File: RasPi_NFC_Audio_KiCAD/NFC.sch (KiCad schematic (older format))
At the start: 31 parts, among them U2 PN532, Y1 Oscillator

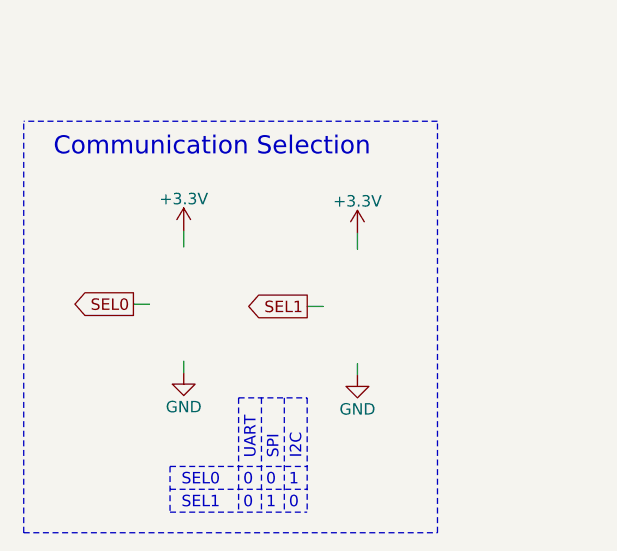
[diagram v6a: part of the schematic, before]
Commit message: Schematic updates
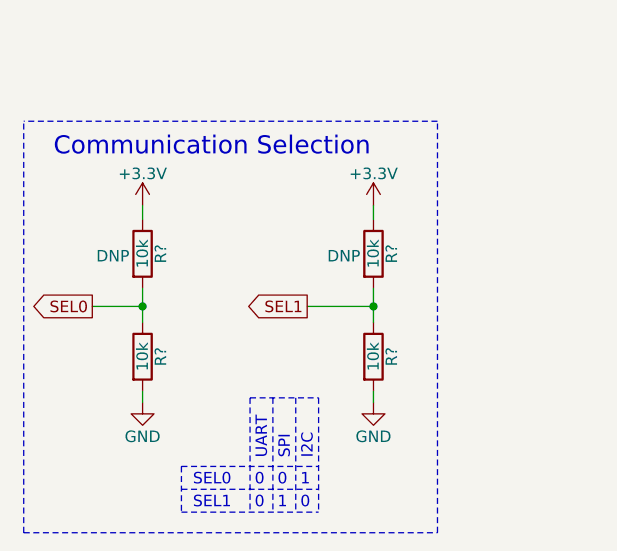
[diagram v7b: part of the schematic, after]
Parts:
- added R? (x4): 10k, Resistors_SMD:R_0603_HandSoldering, symbol Device:R
- L1, L2: DigiKey (none) -> 445-174193-1-ND; Part # (none) -> MLJ1608WR56JT000
- R6: DigiKey (none) -> 311-1.0KGRCT-ND; Part # (none) -> RC0603JR-071KL
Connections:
- wire segments 138 -> 142
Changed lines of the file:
@@
 EESchema Schematic File Version 4
 LIBS:RasPi_NFC_Audio_KiCAD-cache
-EELAYER 29 0
+EELAYER 30 0
 EELAYER END
 $Descr A4 11693 8268
@@
 F 2 "Inductors_SMD:L_0603_HandSoldering" H 8300 3440 50  0001 C CNN
 F 3 "" H 8300 3440 50  0001 C CNN
+F 4 "MLJ1608WR56JT000" H 8300 3440 50  0001 C CNN "Part #"
+F 5 "445-174193-1-ND" H 8300 3440 50  0001 C CNN "DigiKey"
 	1    8300 3440
 	0    -1   -1   0
@@
 F 2 "Inductors_SMD:L_0603_HandSoldering" H 8300 4390 50  0001 C CNN
 F 3 "" H 8300 4390 50  0001 C CNN
+F 4 "MLJ1608WR56JT000" H 8300 4390 50  0001 C CNN "Part #"
+F 5 "445-174193-1-ND" H 8300 4390 50  0001 C CNN "DigiKey"
 	1    8300 4390
 	0    -1   -1   0
@@
 F 2 "Resistors_SMD:R_0603_HandSoldering" V 7680 3090 50  0001 C CNN
 F 3 "" H 7750 3090 50  0001 C CNN
+F 4 "RC0603JR-071KL" H 7750 3090 50  0001 C CNN "Part #"
+F 5 "311-1.0KGRCT-ND" H 7750 3090 50  0001 C CNN "DigiKey"
 	1    7750 3090
 	0    1    1    0
@@
 Text GLabel 5250 3040 0    50   Input ~ 0
 SEL1
-Text GLabel 2160 6430 0    50   Output ~ 0
+Text GLabel 1980 6440 0    50   Output ~ 0
 SEL0
 $Comp
 L power:GND #PWR0127
 U 1 1 5E1B7458
-P 2380 6730
-F 0 "#PWR0127" H 2380 6480 50  0001 C CNN
-F 1 "GND" H 2380 6580 50  0000 C CNN
-F 2 "" H 2380 6730 50  0001 C CNN
-F 3 "" H 2380 6730 50  0001 C CNN
-	1    2380 6730
+P 2200 6860
+F 0 "#PWR0127" H 2200 6610 50  0001 C CNN
+F 1 "GND" H 2200 6710 50  0000 C CNN
+F 2 "" H 2200 6860 50  0001 C CNN
+F 3 "" H 2200 6860 50  0001 C CNN
+	1    2200 6860
 	1    0    0    -1
 $EndComp
@@
 L power:+3.3V #PWR0128
 U 1 1 5E1B7781
-P 2380 6110
-F 0 "#PWR0128" H 2380 5960 50  0001 C CNN
-F 1 "+3.3V" H 2380 6250 50  0000 C CNN
-F 2 "" H 2380 6110 50  0001 C CNN
-F 3 "" H 2380 6110 50  0001 C CNN
-	1    2380 6110
-	1    0    0    -1
-$EndComp
-Wire Wire Line
-	2160 6430 2230 6430
-Wire Wire Line
-	2380 6180 2380 6110
-Wire Wire Line
-	2380 6680 2380 6730
+P 2200 6000
+F 0 "#PWR0128" H 2200 5850 50  0001 C CNN
+F 1 "+3.3V" H 2200 6140 50  0000 C CNN
+F 2 "" H 2200 6000 50  0001 C CNN
+F 3 "" H 2200 6000 50  0001 C CNN
+	1    2200 6000
+	1    0    0    -1
+$EndComp
 Text GLabel 2920 6440 0    50   Output ~ 0
 SEL1
-$Comp
-L power:GND #PWR0129
-U 1 1 5E1D407F
-P 3140 6740
-F 0 "#PWR0129" H 3140 6490 50  0001 C CNN
-F 1 "GND" H 3140 6590 50  0000 C CNN
-F 2 "" H 3140 6740 50  0001 C CNN
-F 3 "" H 3140 6740 50  0001 C CNN
-	1    3140 6740
-	1    0    0    -1
-$EndComp
-$Comp
-L power:+3.3V #PWR0130
-U 1 1 5E1D4089
-P 3140 6120
-F 0 "#PWR0130" H 3140 5970 50  0001 C CNN
-F 1 "+3.3V" H 3140 6260 50  0000 C CNN
-F 2 "" H 3140 6120 50  0001 C CNN
-F 3 "" H 3140 6120 50  0001 C CNN
-	1    3140 6120
-	1    0    0    -1
-$EndComp
-Wire Wire Line
-	2920 6440 2990 6440
-Wire Wire Line
-	3140 6190 3140 6120
-Wire Wire Line
-	3140 6690 3140 6740
-Wire Notes Line
-	2320 7140 2320 7340
-Wire Notes Line
-	2320 7140 2920 7140
-Wire Notes Line
-	2320 7240 2920 7240
-Wire Notes Line
-	2320 7340 2920 7340
-Wire Notes Line
-	2620 6840 2920 6840
-Wire Notes Line
-	2620 6840 2620 7340
-Wire Notes Line
-	2920 6840 2920 7340
-Wire Notes Line
-	2820 6840 2820 7340
-Wire Notes Line
-	2720 6840 2720 7340
-Text Notes 2370 7230 0    50   ~ 0
+Wire Notes Line
+	2370 7140 2370 7340
+Wire Notes Line
+	2370 7140 2970 7140
+Wire Notes Line
+	2370 7240 2970 7240
+Wire Notes Line
+	2370 7340 2970 7340
+Wire Notes Line
+	2670 6840 2970 6840
+Wire Notes Line
+	2670 6840 2670 7340
+Wire Notes Line
+	2970 6840 2970 7340
+Wire Notes Line
+	2870 6840 2870 7340
+Wire Notes Line
+	2770 6840 2770 7340
+Text Notes 2420 7230 0    50   ~ 0
 SEL0
-Text Notes 2370 7330 0    50   ~ 0
+Text Notes 2420 7330 0    50   ~ 0
 SEL1
-Text Notes 2640 7330 0    50   ~ 0
+Text Notes 2690 7330 0    50   ~ 0
 0
-Text Notes 2640 7230 0    50   ~ 0
+Text Notes 2690 7230 0    50   ~ 0
 0
-Text Notes 2740 7230 0    50   ~ 0
+Text Notes 2790 7230 0    50   ~ 0
 0
-Text Notes 2840 7330 0    50   ~ 0
+Text Notes 2890 7330 0    50   ~ 0
 0
-Text Notes 2740 7330 0    50   ~ 0
+Text Notes 2790 7330 0    50   ~ 0
 1
-Text Notes 2840 7230 0    50   ~ 0
+Text Notes 2890 7230 0    50   ~ 0
 1
-Text Notes 2700 7110 1    50   ~ 0
+Text Notes 2750 7110 1    50   ~ 0
 UART
-Text Notes 2800 7110 1    50   ~ 0
+Text Notes 2850 7110 1    50   ~ 0
 SPI
-Text Notes 2900 7110 1    50   ~ 0
+Text Notes 2950 7110 1    50   ~ 0
 I2C
 Wire Notes Line
@@
 	1    0    0    -1
 $EndComp
+$Comp
+L Device:R R?
+U 1 1 5E1D07E5
+P 2200 6660
+F 0 "R?" V 2280 6660 50  0000 C CNN
+F 1 "10k" V 2200 6660 50  0000 C CNN
+F 2 "Resistors_SMD:R_0603_HandSoldering" V 2130 6660 50  0001 C CNN
+F 3 "" H 2200 6660 50  0001 C CNN
+F 4 "RNCP0603FTD10K0" H 2200 6660 50  0001 C CNN "Part #"
+F 5 "RNCP0603FTD10K0CT-ND" H 2200 6660 50  0001 C CNN "DigiKey"
+	1    2200 6660
+	1    0    0    -1
+$EndComp
+$Comp
+L Device:R R?
+U 1 1 5E1D2BE3
+P 2200 6210
+F 0 "R?" V 2280 6210 50  0000 C CNN
+F 1 "10k" V 2200 6210 50  0000 C CNN
+F 2 "Resistors_SMD:R_0603_HandSoldering" V 2130 6210 50  0001 C CNN
+F 3 "" H 2200 6210 50  0001 C CNN
+F 4 "RNCP0603FTD10K0" H 2200 6210 50  0001 C CNN "Part #"
+F 5 "RNCP0603FTD10K0CT-ND" H 2200 6210 50  0001 C CNN "DigiKey"
+F 6 "DNP" H 2070 6200 50  0000 C CNN "DNP"
+	1    2200 6210
+	1    0    0    -1
+$EndComp
+Wire Wire Line
+	2200 6000 2200 6060
+Wire Wire Line
+	2200 6360 2200 6440
+Wire Wire Line
+	1980 6440 2200 6440
+Connection ~ 2200 6440
+Wire Wire Line
+	2200 6440 2200 6510
+$Comp
+L power:GND #PWR?
+U 1 1 5E1FB945
+P 3210 6860
+F 0 "#PWR?" H 3210 6610 50  0001 C CNN
+F 1 "GND" H 3210 6710 50  0000 C CNN
+F 2 "" H 3210 6860 50  0001 C CNN
+F 3 "" H 3210 6860 50  0001 C CNN
+	1    3210 6860
+	1    0    0    -1
+$EndComp
+$Comp
+L power:+3.3V #PWR?
+U 1 1 5E1FB94B
+P 3210 6000
+F 0 "#PWR?" H 3210 5850 50  0001 C CNN
+F 1 "+3.3V" H 3210 6140 50  0000 C CNN
+F 2 "" H 3210 6000 50  0001 C CNN
+F 3 "" H 3210 6000 50  0001 C CNN
+	1    3210 6000
+	1    0    0    -1
+$EndComp
+$Comp
+L Device:R R?
+U 1 1 5E1FB953
+P 3210 6660
+F 0 "R?" V 3290 6660 50  0000 C CNN
+F 1 "10k" V 3210 6660 50  0000 C CNN
+F 2 "Resistors_SMD:R_0603_HandSoldering" V 3140 6660 50  0001 C CNN
+F 3 "" H 3210 6660 50  0001 C CNN
+F 4 "RNCP0603FTD10K0" H 3210 6660 50  0001 C CNN "Part #"
+F 5 "RNCP0603FTD10K0CT-ND" H 3210 6660 50  0001 C CNN "DigiKey"
+	1    3210 6660
+	1    0    0    -1
+$EndComp
+$Comp
+L Device:R R?
+U 1 1 5E1FB95C
+P 3210 6210
+F 0 "R?" V 3290 6210 50  0000 C CNN
+F 1 "10k" V 3210 6210 50  0000 C CNN
+F 2 "Resistors_SMD:R_0603_HandSoldering" V 3140 6210 50  0001 C CNN
+F 3 "" H 3210 6210 50  0001 C CNN
+F 4 "RNCP0603FTD10K0" H 3210 6210 50  0001 C CNN "Part #"
+F 5 "RNCP0603FTD10K0CT-ND" H 3210 6210 50  0001 C CNN "DigiKey"
+F 6 "DNP" H 3080 6200 50  0000 C CNN "DNP"
+	1    3210 6210
+	1    0    0    -1
+$EndComp
+Wire Wire Line
+	3210 6000 3210 6060
+Wire Wire Line
+	3210 6360 3210 6440
+Connection ~ 3210 6440
+Wire Wire Line
+	3210 6440 3210 6510
+Wire Wire Line
+	2920 6440 3210 6440
+Wire Wire Line
+	2200 6810 2200 6860
+Wire Wire Line
+	3210 6810 3210 6860
 $EndSCHEMATC

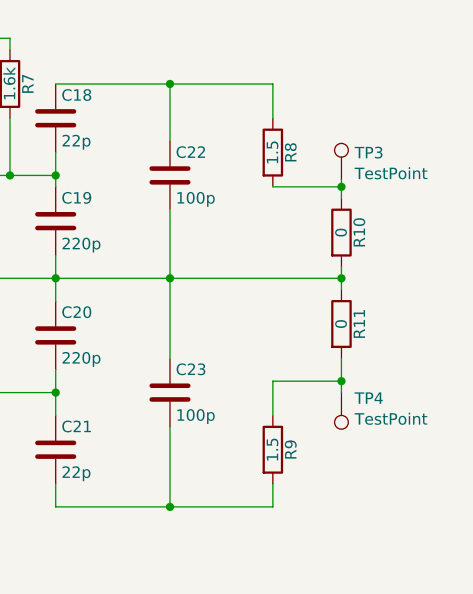
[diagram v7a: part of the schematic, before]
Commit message: Schematic updates
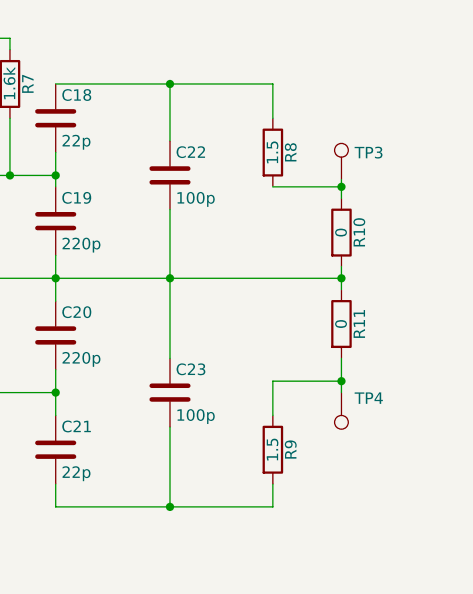
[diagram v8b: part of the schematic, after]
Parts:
- C17: DigiKey (none) -> 399-1083-1-ND; Part # (none) -> C0603C102J5RACTU
- C18, C21: DigiKey (none) -> 399-7874-1-ND; Part # (none) -> C0603C220J1GACTU
- C19, C20: DigiKey (none) -> 311-1073-1-ND; Part # (none) -> CC0603JRNPO9BN221
- C22, C23: DigiKey (none) -> 311-1069-1-ND; Part # (none) -> CC0603JRNPO9BN101
- R10, R11: DigiKey (none) -> 311-0.0GRCT-ND; Part # (none) -> RC0603JR-070RL
- R7: DigiKey (none) -> 311-1.60KHRCT-ND; Part # (none) -> RC0603FR-071K6L
- R8, R9: DigiKey (none) -> RMCF0603FT1R50CT-ND; Part # (none) -> RMCF0603FT1R50
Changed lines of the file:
@@
 EESchema Schematic File Version 4
 LIBS:RasPi_NFC_Audio_KiCAD-cache
-EELAYER 30 0
+EELAYER 29 0
 EELAYER END
 $Descr A4 11693 8268
@@
 F 2 "Capacitors_SMD:C_0402" H 8738 3490 50  0001 C CNN
 F 3 "" H 8700 3640 50  0001 C CNN
+F 4 "CC0603JRNPO9BN221" H 8700 3640 50  0001 C CNN "Part #"
+F 5 "311-1073-1-ND" H 8700 3640 50  0001 C CNN "DigiKey"
 	1    8700 3640
 	1    0    0    -1
@@
 F 2 "Capacitors_SMD:C_0402" H 8738 3990 50  0001 C CNN
 F 3 "" H 8700 4140 50  0001 C CNN
+F 4 "CC0603JRNPO9BN221" H 8700 4140 50  0001 C CNN "Part #"
+F 5 "311-1073-1-ND" H 8700 4140 50  0001 C CNN "DigiKey"
 	1    8700 4140
 	1    0    0    -1
@@
 F 2 "Capacitors_SMD:C_0402" H 8738 3040 50  0001 C CNN
 F 3 "" H 8700 3190 50  0001 C CNN
+F 4 "C0603C220J1GACTU" H 8700 3190 50  0001 C CNN "Part #"
+F 5 "399-7874-1-ND" H 8700 3190 50  0001 C CNN "DigiKey"
 	1    8700 3190
 	1    0    0    -1
@@
 F 2 "Capacitors_SMD:C_0402" H 8738 4490 50  0001 C CNN
 F 3 "" H 8700 4640 50  0001 C CNN
+F 4 "C0603C220J1GACTU" H 8700 4640 50  0001 C CNN "Part #"
+F 5 "399-7874-1-ND" H 8700 4640 50  0001 C CNN "DigiKey"
 	1    8700 4640
 	1    0    0    -1
@@
 F 2 "Capacitors_SMD:C_0402" H 9238 4240 50  0001 C CNN
 F 3 "" H 9200 4390 50  0001 C CNN
+F 4 "CC0603JRNPO9BN101" H 9200 4390 50  0001 C CNN "Part #"
+F 5 "311-1069-1-ND" H 9200 4390 50  0001 C CNN "DigiKey"
 	1    9200 4390
 	1    0    0    -1
@@
 F 2 "Capacitors_SMD:C_0402" H 9238 3290 50  0001 C CNN
 F 3 "" H 9200 3440 50  0001 C CNN
+F 4 "CC0603JRNPO9BN101" H 9200 3440 50  0001 C CNN "Part #"
+F 5 "311-1069-1-ND" H 9200 3440 50  0001 C CNN "DigiKey"
 	1    9200 3440
 	1    0    0    -1
@@
 F 2 "Resistors_SMD:R_0603_HandSoldering" V 9580 4640 50  0001 C CNN
 F 3 "" H 9650 4640 50  0001 C CNN
+F 4 "RMCF0603FT1R50" H 9650 4640 50  0001 C CNN "Part #"
+F 5 "RMCF0603FT1R50CT-ND" H 9650 4640 50  0001 C CNN "DigiKey"
 	1    9650 4640
 	1    0    0    -1
@@
 F 2 "Resistors_SMD:R_0603_HandSoldering" V 9580 3340 50  0001 C CNN
 F 3 "" H 9650 3340 50  0001 C CNN
+F 4 "RMCF0603FT1R50" H 9650 3340 50  0001 C CNN "Part #"
+F 5 "RMCF0603FT1R50CT-ND" H 9650 3340 50  0001 C CNN "DigiKey"
 	1    9650 3340
 	1    0    0    -1
@@
 F 2 "Resistors_SMD:R_0402" V 9880 3690 50  0001 C CNN
 F 3 "" H 9950 3690 50  0001 C CNN
+F 4 "RC0603JR-070RL" H 9950 3690 50  0001 C CNN "Part #"
+F 5 "311-0.0GRCT-ND" H 9950 3690 50  0001 C CNN "DigiKey"
 	1    9950 3690
 	1    0    0    -1
@@
 F 2 "Resistors_SMD:R_0402" V 9880 4090 50  0001 C CNN
 F 3 "" H 9950 4090 50  0001 C CNN
+F 4 "RC0603JR-070RL" H 9950 4090 50  0001 C CNN "Part #"
+F 5 "311-0.0GRCT-ND" H 9950 4090 50  0001 C CNN "DigiKey"
 	1    9950 4090
 	1    0    0    -1
@@
 F 2 "Resistors_SMD:R_0603_HandSoldering" V 8430 3040 50  0001 C CNN
 F 3 "" H 8500 3040 50  0001 C CNN
+F 4 "RC0603FR-071K6L" H 8500 3040 50  0001 C CNN "Part #"
+F 5 "311-1.60KHRCT-ND" H 8500 3040 50  0001 C CNN "DigiKey"
 	1    8500 3040
 	1    0    0    -1
@@
 F 2 "Capacitors_SMD:C_0402" H 8188 2690 50  0001 C CNN
 F 3 "" H 8150 2840 50  0001 C CNN
+F 4 "C0603C102J5RACTU" H 8150 2840 50  0001 C CNN "Part #"
+F 5 "399-1083-1-ND" H 8150 2840 50  0001 C CNN "DigiKey"
 	1    8150 2840
 	0    -1   -1   0
@@
 P 9950 3460
 F 0 "TP3" H 10008 3578 50  0000 L CNN
-F 1 "TestPoint" H 10008 3487 50  0000 L CNN
+F 1 "TestPoint" H 10008 3487 50  0001 L CNN
 F 2 "" H 10150 3460 50  0001 C CNN
 F 3 "~" H 10150 3460 50  0001 C CNN
@@
 P 9950 4390
 F 0 "TP4" H 9892 4416 50  0000 R CNN
-F 1 "TestPoint" H 9892 4507 50  0000 R CNN
+F 1 "TestPoint" H 9892 4507 50  0001 R CNN
 F 2 "" H 10150 4390 50  0001 C CNN
 F 3 "~" H 10150 4390 50  0001 C CNN
